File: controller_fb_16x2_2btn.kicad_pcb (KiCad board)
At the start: 2 copper layers, 105 x 35.9 mm, 10 parts, among them J1 Conn_01x19, SW1 SW_Push_LED, SW2 SW_Push_LED

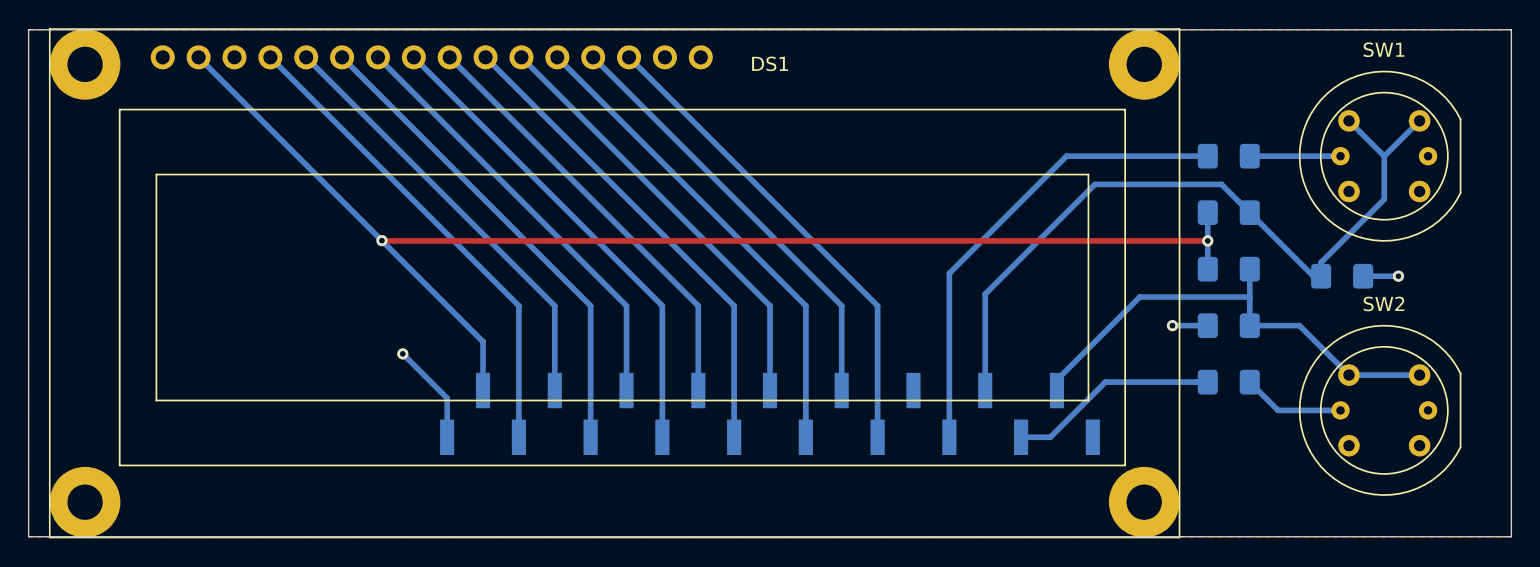
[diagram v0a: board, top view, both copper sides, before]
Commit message: Init v0.2
- Unifying a button connections
- Enlarge button holes
- Decrease PCB high -0.1mm x 2
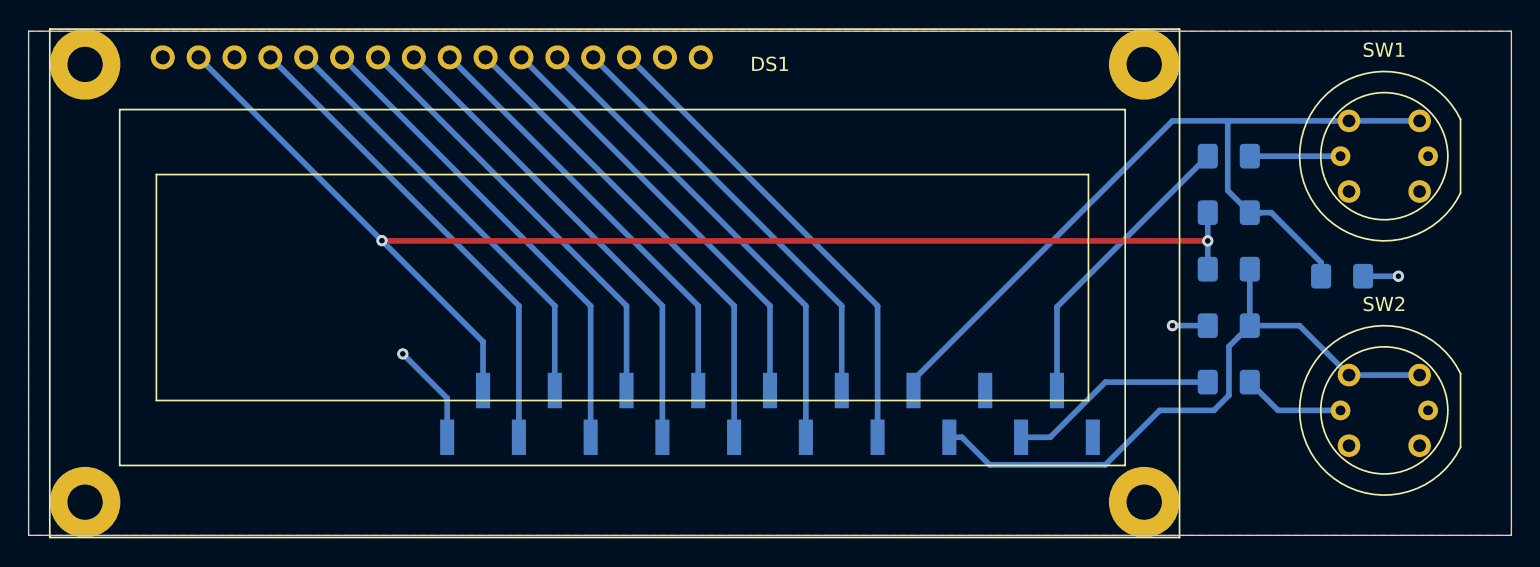
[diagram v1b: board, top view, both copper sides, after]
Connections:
- C1 pad 2: /PB5(INT2) -> /PB3
- C2 pad 2: /PD0 -> /PB4
- J1 pad 14: (no net) -> /PB3
- J1 pad 16: /PB5(INT2) -> (no net)
- R1 pad 2: /PB5(INT2) -> /PB3
- R2 pad 2: /PB4 -> /PD0
- R3 pad 2: /PD0 -> /PB4
- SW1 pad 2: /PB5(INT2) -> /PB3
- SW2 pad 2: /PD0 -> /PB4
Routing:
- net /PB3: track 0.00 -> 58.8 mm
- net /PB5(INT2): track 55.0 -> 0.00 mm
- net /PD0: track 34.3 -> 21.8 mm
- net /PB4: track 33.3 -> 45.7 mm
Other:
- board size 105 x 35.9 mm -> 105 x 35.7 mm

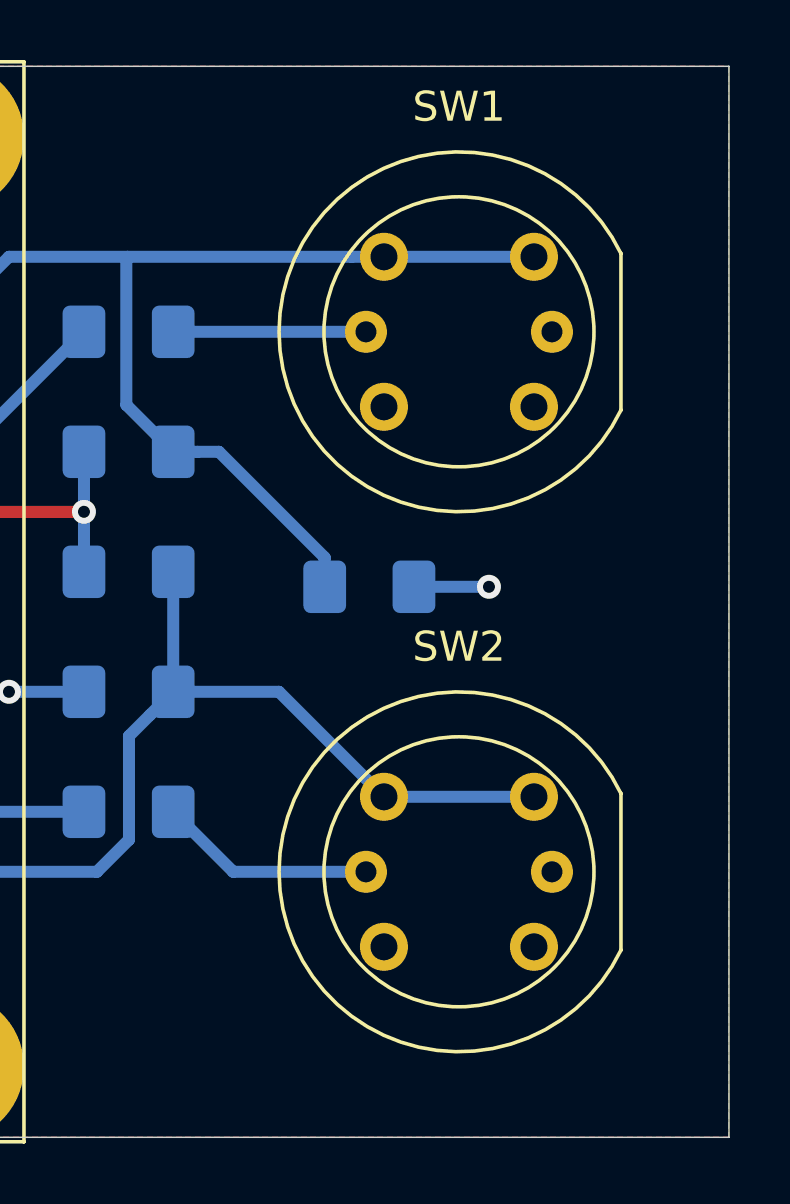
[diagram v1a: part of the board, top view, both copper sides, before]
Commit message: Zmiana rozmaru otworów przycisków
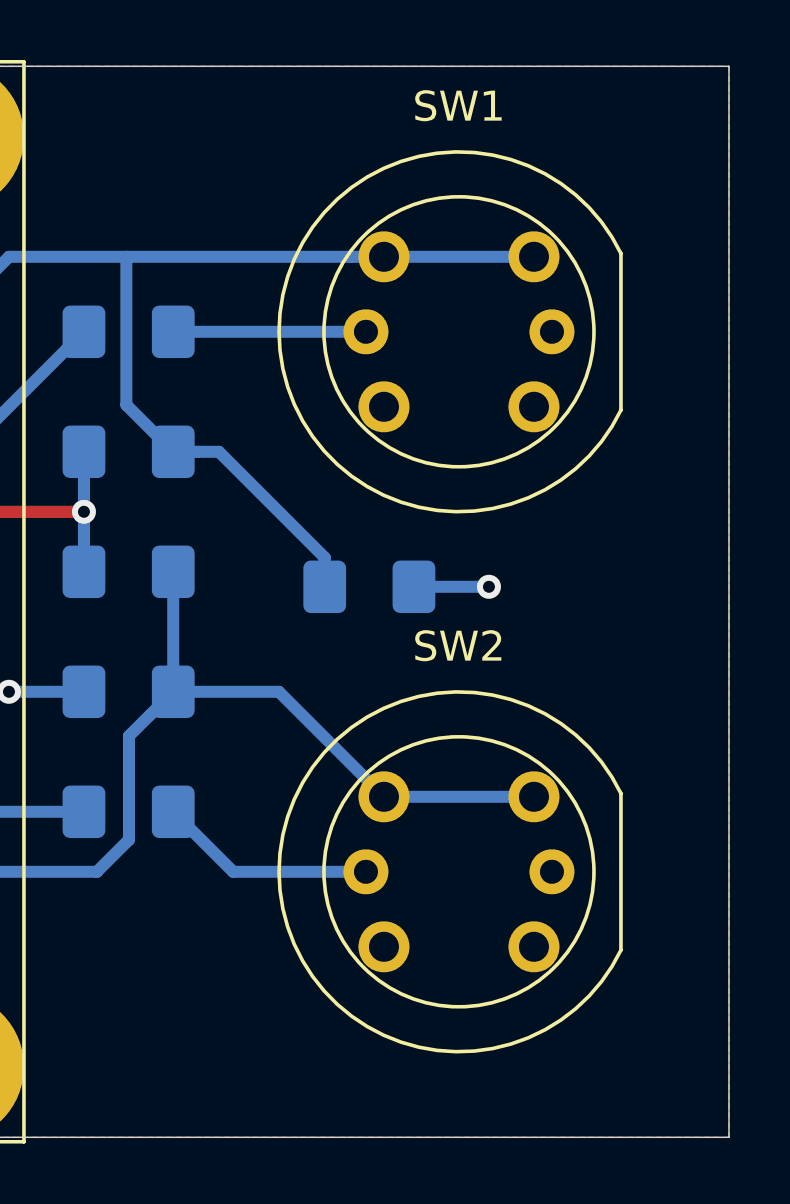
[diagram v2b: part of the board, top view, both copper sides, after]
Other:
- net class Default removed
